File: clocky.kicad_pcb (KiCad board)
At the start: 4 copper layers, 93.9 x 45.6 mm, 79 parts, among them J1 Bot 50 pin, J2 Bot 40 pin, J3 Top 50 pin, J4 Top 40 pin, J5 Power, J6 CAP, J8 Skedd, U1 HEF4094B, U10 TMP117xxDRV, U11 ENS220, U2 HEF4094B, U3 HEF4094B, U4 HEF4094B, U5 HEF4094B, U6 HEF4094B, U7 BQ25570, U8 ENS212, U9 STM32U031C8Ux, U98 TMP117xxDRV, U99 TMP117xxDRV, Y1 32768Hz

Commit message: Manufacturing updates.
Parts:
- R25: value 330k -> 560k
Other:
- outline, holes or cut-outs redrawn

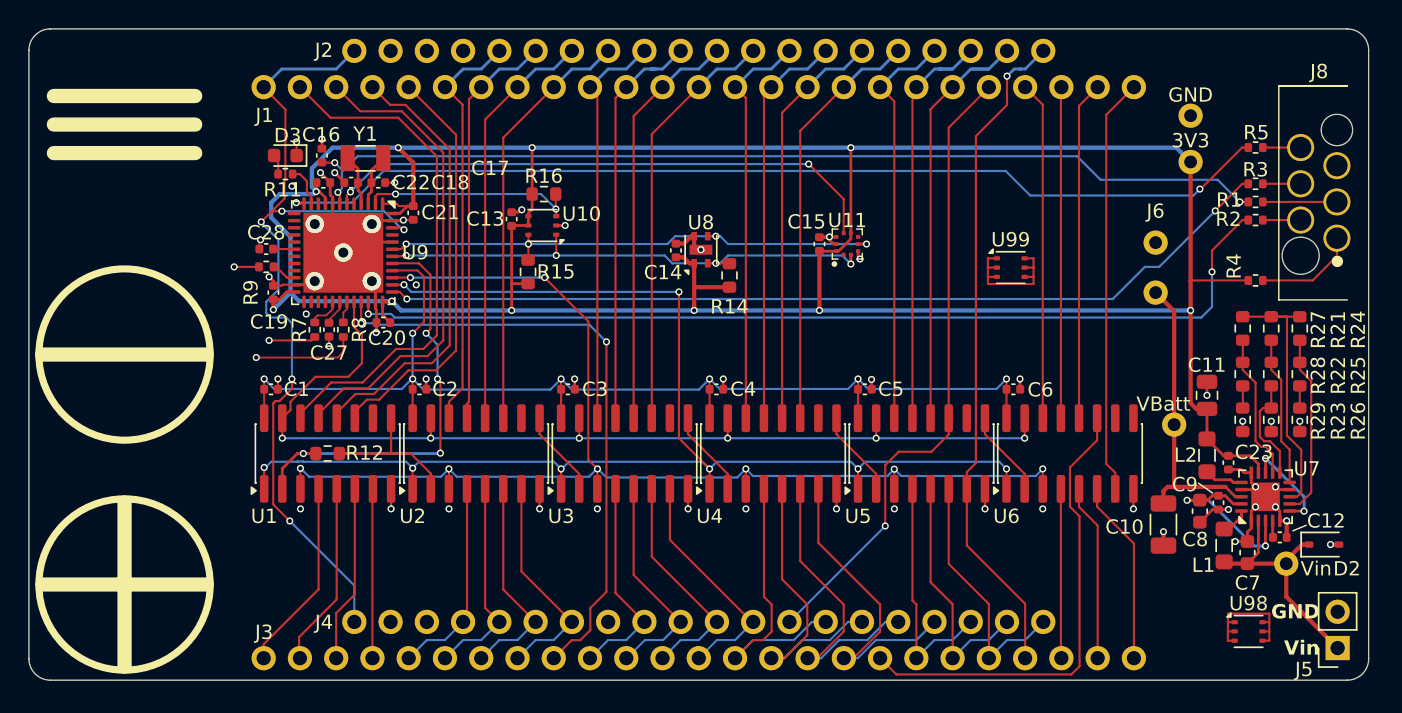
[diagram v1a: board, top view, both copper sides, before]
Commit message: Update board with 1.8V power domain.
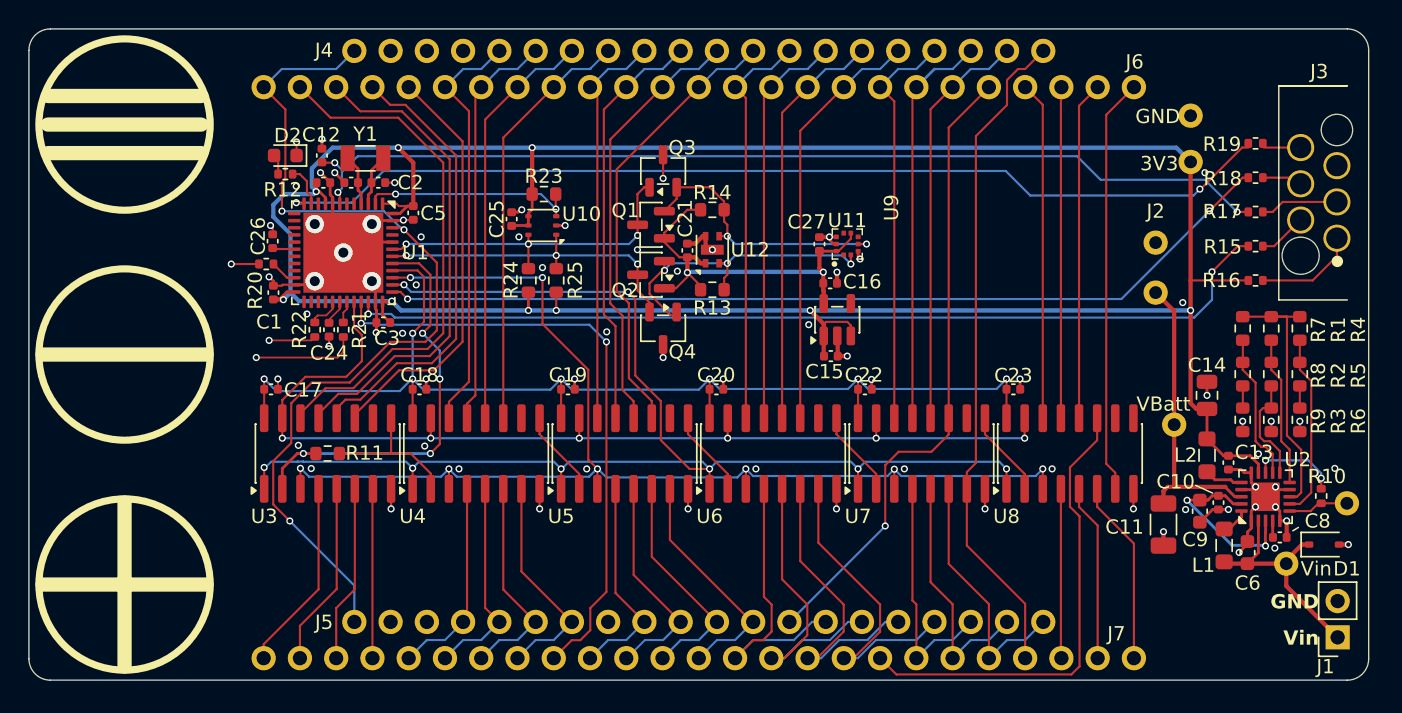
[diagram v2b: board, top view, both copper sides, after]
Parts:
- removed U98, U99: TMP117xxDRV, Parts:WSON-6-1EP_2x2mm_P0.65mm_NoEP
- added C15: 1u, Capacitor_SMD:C_0402_1005Metric, F.Cu at (159.2, 96.3)
- added C16: 1u, Capacitor_SMD:C_0402_1005Metric, F.Cu at (159.2, 91.2)
- added Q1: HL2300, Package_TO_SOT_SMD:SOT-23, F.Cu at (146.7, 87.1)
- added Q2: HL2300, Package_TO_SOT_SMD:SOT-23, F.Cu at (146.7, 90.6)
- added Q3: JFET, Package_TO_SOT_SMD:SOT-23-3, F.Cu at (147.5, 83.3)
- added Q4: JFET, Package_TO_SOT_SMD:SOT-23-3, F.Cu at (147.5, 94.3)
- added R10: 100k, Resistor_SMD:R_0402_1005Metric, F.Cu at (193.6, 106.1)
- added R13: 33k, Resistor_SMD:R_0603_1608Metric, F.Cu at (150.9, 91.7)
- added R14: 33k, Resistor_SMD:R_0603_1608Metric, F.Cu at (150.9, 86.0)
- added TP2: TestPoint_Probe, Parts:TestPoint, F.Cu at (195.4, 106.6)
- added U9: TPS7A0218DBV, Package_TO_SOT_SMD:SOT-23-5, F.Cu at (159.7, 93.8)
- R5: renamed from R25; value 560k -> 430k
- TP6: renamed from TP3; moved to B.Cu
- moved R25 12.1 mm to (140.0, 91.0)
- moved R15 1.83 mm to (189.0, 88.6)
- moved C21 0.80 mm to (149.2, 88.9)
- moved U12 0.80 mm to (150.9, 88.8)
- moved J1 0.75 mm to (194.8, 116.0)
- moved C26 0.71 mm to (120.2, 88.2), turned to 90 degrees
- moved R17 0.70 mm to (189.0, 86.2)
- moved R24 0.60 mm to (138.1, 91.0)
- moved R18 0.43 mm to (189.0, 83.8)
- moved R19 0.29 mm to (189.0, 81.4)
- moved TP6 0.28 mm to (117.2, 89.9)
- moved R20 0.20 mm to (119.7, 89.8)
- renumbered C19 to C1, C9 to C10, C10 to C11, C16 to C12, C23 to C13, C11 to C14, C1 to C17, C2 to C18, C3 to C19, C17 to C2, C4 to C20, C14 to C21, C5 to C22, C6 to C23, C27 to C24, C13 to C25, C28 to C26, C15 to C27, C20 to C3, C18 to C4, C21 to C5, C7 to C6, C22 to C7, C12 to C8, C8 to C9, D2 to D1, D3 to D2, J5 to J1, J6 to J2, J8 to J3, J2 to J4, J4 to J5, J1 to J6, J3 to J7, R21 to R1, R12 to R11, R11 to R12, R2 to R15, R4 to R16, R1 to R17, R3 to R18, R5 to R19, R22 to R2, R9 to R20, R8 to R21, R7 to R22, R16 to R23, R15 to R24, R14 to R25, R23 to R3, R24 to R4, R26 to R6, R27 to R7, R28 to R8, R29 to R9, TP7 to TP1, TP5 to TP3, TP6 to TP4, TP4 to TP5, TP2 to TP7, TP1 to TP8, U9 to U1, U8 to U12, U7 to U2, U1 to U3, U2 to U4, U3 to U5, U4 to U6, U5 to U7, U6 to U8
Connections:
- C21 pad 1: +3V3 -> +1V8
- C27 pad 1: +3V3 -> +1V8
- U1 pad 6: /Press -> unconnected-(U1-PF1-Pad6)
- U11 pad 10: +3V3 -> +1V8
- U11 pad 2: /SCL -> /SCLl
- U11 pad 4: /SDA -> /SDAl
- U11 pad 6: +3V3 -> +1V8
- U11 pad 7: /Press -> unconnected-(U11-INT-Pad7)
- U12 pad 1: +3V3 -> +1V8
- U12 pad 2: /SCL -> /SCLl
- U12 pad 3: /SDA -> /SDAl
- U2 pad 6: /VBatOK -> Net-(U2-VOUT_EN)
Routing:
- net /Press: track 39.7 -> 0.00 mm, vias 2 -> 0
- net +1V8: track 0.00 -> 28.3 mm, vias 0 -> 2
- net /SCLl: track 0.00 -> 22.3 mm, vias 0 -> 3
- net +3V3: track 218.7 -> 199.0 mm, vias 10 -> 9
- net /SDAl: track 0.00 -> 19.4 mm, vias 0 -> 2
- net /SDA: track 36.7 -> 23.8 mm, vias 4 -> 3
- net /SCL: track 36.4 -> 23.7 mm, vias 4 -> 3
- net Net-(U99-ADD0): track 10.5 -> 0.00 mm
- net Net-(U98-ADD0): track 9.55 -> 0.00 mm
- net Net-(U2-VOUT_EN): track 0.00 -> 4.24 mm
- net /COM: track 62.1 -> 65.3 mm, vias 5 -> 3
- net GND: track 67.9 -> 71.0 mm, vias 54 -> 74
- net /ExtraPad: track 14.9 -> 12.5 mm
- net /Q3P: track 29.4 -> 31.5 mm
- net /SWDIO: track 67.7 -> 65.8 mm
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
